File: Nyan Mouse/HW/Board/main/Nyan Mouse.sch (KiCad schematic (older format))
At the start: 11 parts, among them M101 BATTBALANCE-2S, P101 CONN_20X2, P102 CONN_4, P103 CONN_2, P104 CONN_2, U101 DRV8837, U102 DRV8837

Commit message: Finalized connector structure.
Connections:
- net +3.3VA: now also P101.1 (P1), P101.3 (P3), P101.5 (P5); no longer P101.19 (P19), P101.21 (P21), P101.23 (P23)
- net +3.3VD: now also P101.2 (P2), P101.4 (P4), P101.6 (P6); no longer P101.36 (P36), P101.38 (P38), P101.40 (P40)
- net AGND: now also P101.35 (P35), P101.37 (P37); no longer P101.25
- net DGND: now also P101.36 (P36), P101.38 (P38), P101.40 (P40); no longer P101.1 (P1), P101.3 (P3), P101.5 (P5)
- net connectors and lights/RCLK: now also P101.16 (P16); no longer P101.8 (P8)
- net connectors and lights/SCLK: now also P101.14 (P14); no longer P101.6 (P6)
- net connectors and lights/SDI: now also P101.12 (P12); no longer P101.4 (P4)
- net connectors and lights/nOE: now also P101.10 (P10); no longer P101.2 (P2)
- net re1: now also P101.21 (P21); no longer P101.27 (P27)
- net re2: now also P101.23 (P23); no longer P101.29 (P29)
- net re3: now also P101.25; no longer P101.31 (P31)
- net re4: now also P101.27 (P27); no longer P101.33 (P33)
- net re5: now also P101.29 (P29); no longer P101.35 (P35)
- net re6: now also P101.31 (P31); no longer P101.37 (P37)
- net at P101.11 (P11): no longer U102.6 (IN1)
- net at P102.3 (P3): now also P101.18 (P18); no longer P101.12 (P12)
- net at P101.13 (P13): no longer U102.5 (IN2)
- net at P102.4 (P4): now also P101.20 (P20); no longer P101.14 (P14)
- net at P101.28 (P28): now also U101.6 (IN1)
- net at P101.30 (P30): now also U101.5 (IN2)
- net at P101.32 (P32): now also U102.6 (IN1)
- net at P101.34 (P34): now also U102.5 (IN2)
- net at P101.7 (P7): no longer U101.6 (IN1)
- net at P101.9 (P9): no longer U101.5 (IN2)
- new net gyro_a: P101.33 (P33)
- no-connect marks 14 -> 8
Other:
- moved on the sheet: C101, C102, L101, M101, P102, P103, P104, R101, U101, U102

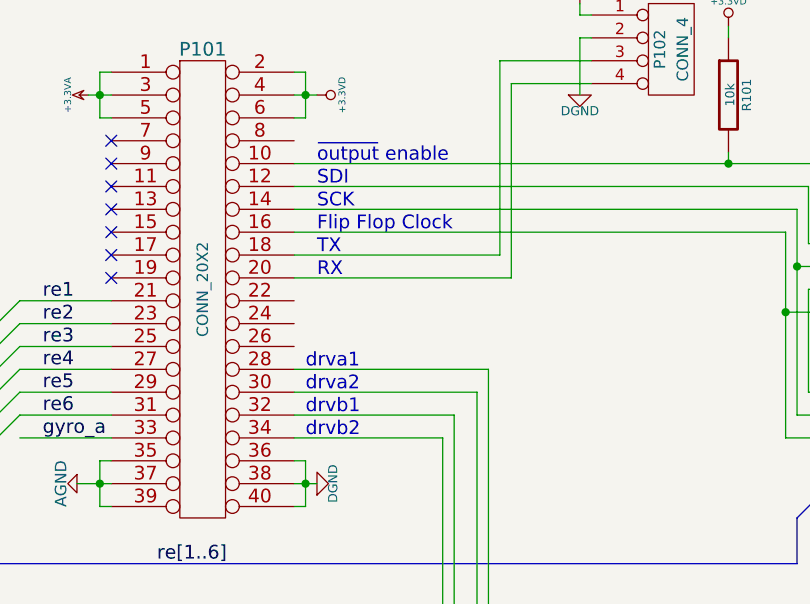
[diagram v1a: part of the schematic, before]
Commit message: Okay, now the connector is finalized.
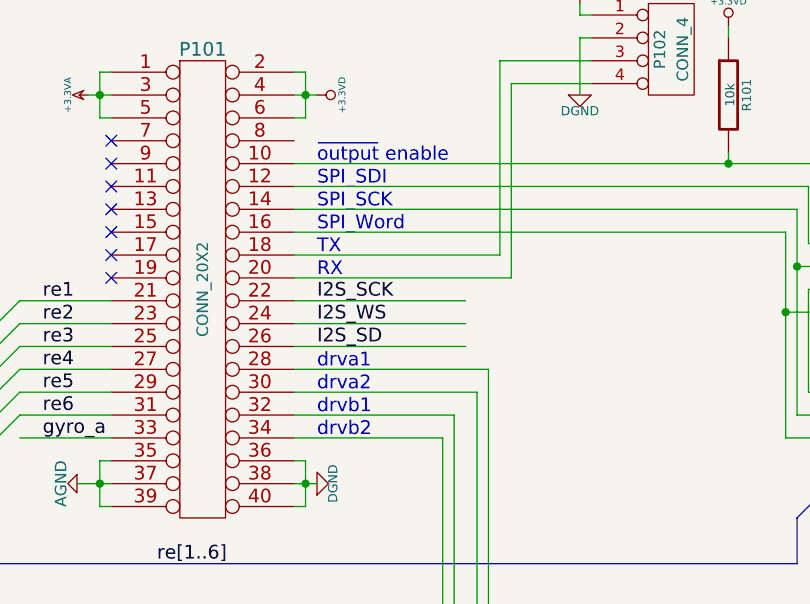
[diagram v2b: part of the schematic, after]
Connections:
- net labels added: I2S_SCK, I2S_SD, I2S_WS
- wire segments 109 -> 112
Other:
- note added: "SPI_SCK"
- note added: "SPI_SDI"
- note added: "SPI_Word"
- note removed: "Flip Flop Clock"
- note removed: "SCK"
- note removed: "SDI"
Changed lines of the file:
@@
 ~output enable
 Text Notes 6500 2100 0    60   ~ 0
-SDI
+SPI_SDI
 Text Notes 6500 2200 0    60   ~ 0
-SCK
+SPI_SCK
 Text Notes 6500 2300 0    60   ~ 0
-Flip Flop Clock
+SPI_Word
 Text Label 5300 2600 0    60   ~ 0
 re1
@@
 Wire Wire Line
 	9250 5950 9250 6000
-Text Notes 6450 3200 0    60   ~ 0
+Text Notes 6500 3200 0    60   ~ 0
 drvb2
-Text Notes 6450 3100 0    60   ~ 0
+Text Notes 6500 3100 0    60   ~ 0
 drvb1
-Text Notes 6450 3000 0    60   ~ 0
+Text Notes 6500 3000 0    60   ~ 0
 drva2
-Text Notes 6450 2900 0    60   ~ 0
+Text Notes 6500 2900 0    60   ~ 0
 drva1
 $Comp
@@
 NoConn ~ 5600 2400
 NoConn ~ 5600 2500
+Wire Wire Line
+	6400 2600 7150 2600
+Wire Wire Line
+	6400 2700 7150 2700
+Wire Wire Line
+	6400 2800 7150 2800
+Text Label 6500 2600 0    60   ~ 0
+I2S_SCK
+Text Label 6500 2700 0    60   ~ 0
+I2S_WS
+Text Label 6500 2800 0    60   ~ 0
+I2S_SD
 $EndSCHEMATC

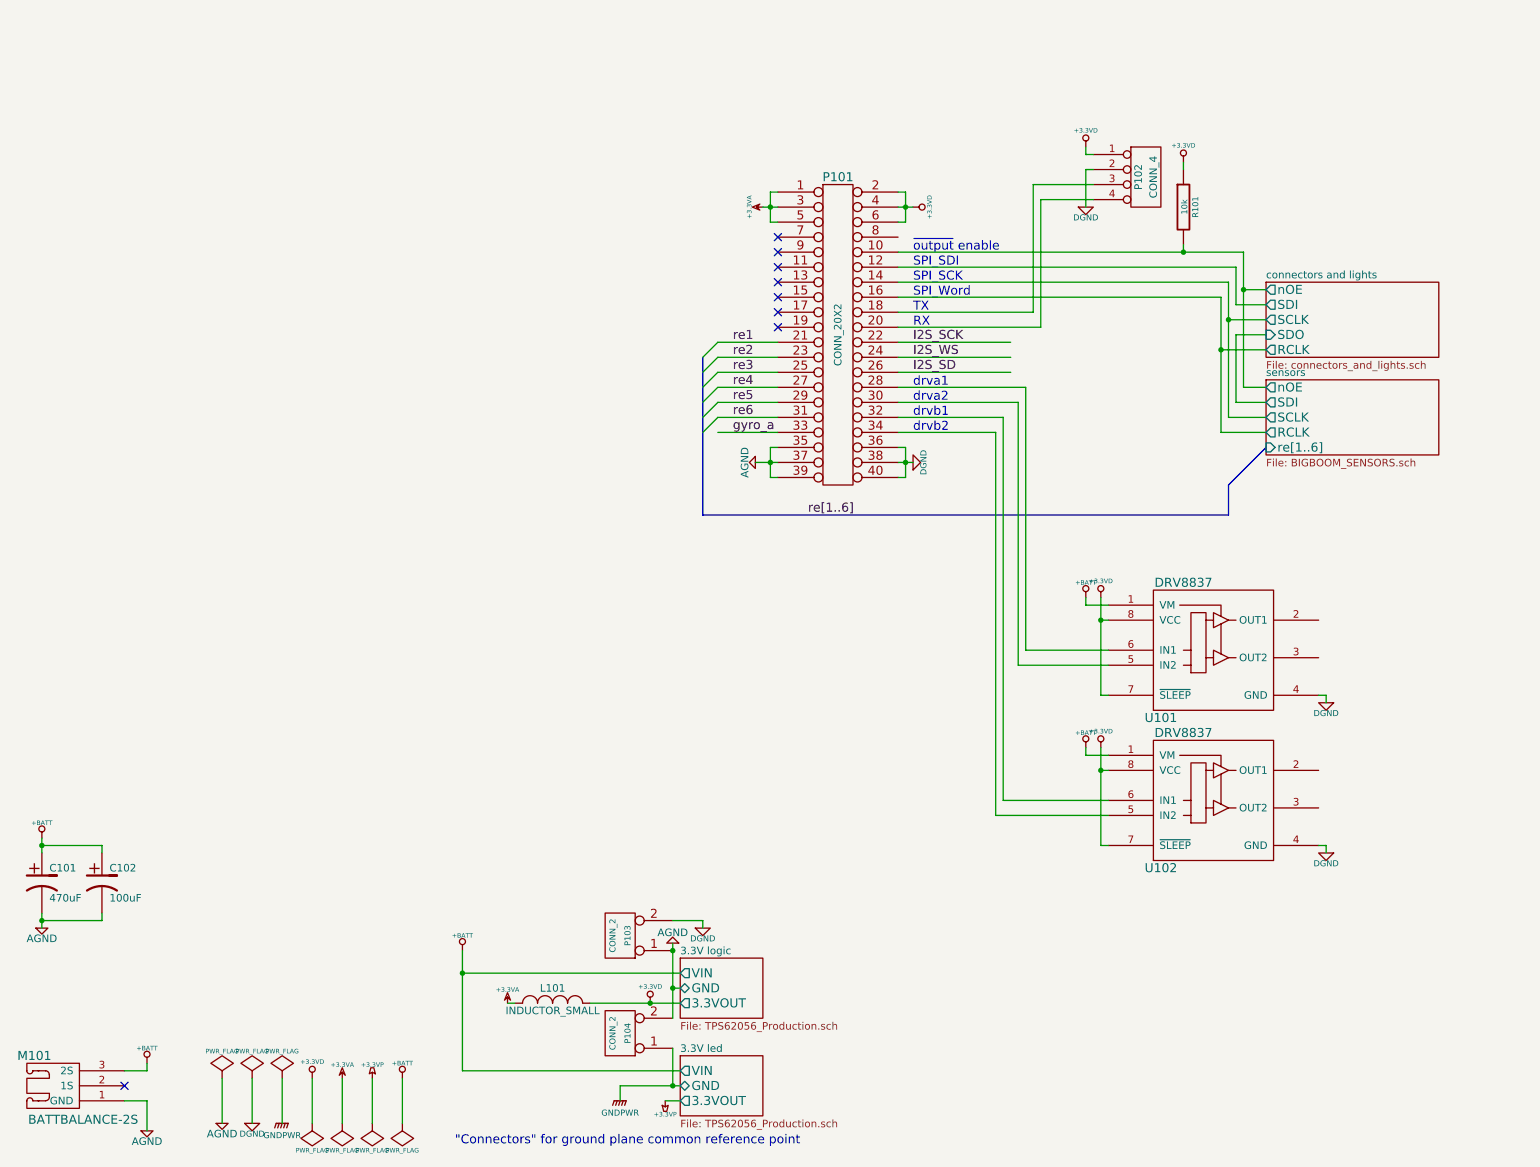
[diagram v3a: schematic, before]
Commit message: Added bank names to FPGA
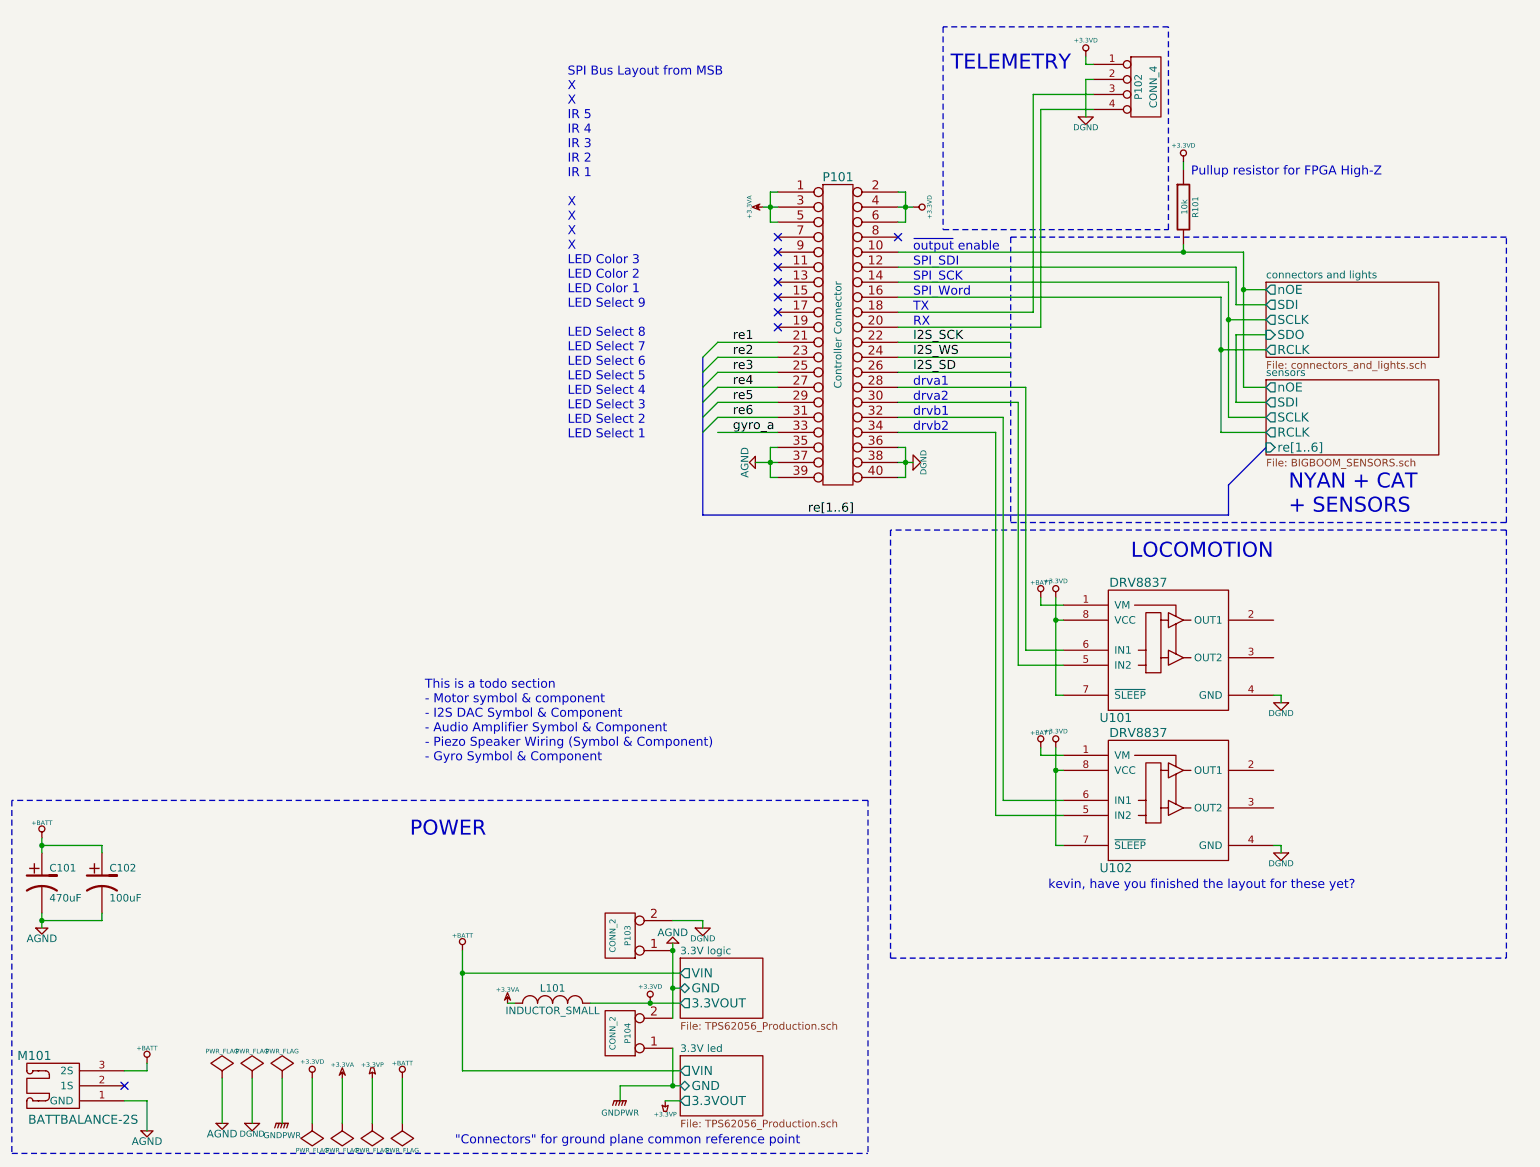
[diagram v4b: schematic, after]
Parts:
- P101: value CONN_20X2 -> Controller Connector
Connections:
- no-connect marks 8 -> 9
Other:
- note added: "LOCOMOTION"
- note added: "NYAN + CAT\n+ SENSORS"
- note added: "POWER"
- note added: "Pullup resistor for FPGA High-Z"
- note added: "SPI Bus Layout from MSB\nX\nX\nIR 5\nIR 4\nIR 3\nIR 2\nIR 1\n\nX\nX\nX\nX\nLED Color 3\nLED Color 2\nLED Color 1\nLED Select 9\n\nLED Select 8\nLED Select 7\nLED Select 6\nLED Select 5\nLED Select 4\nLED Select 3\nLED Select 2\nLED Select 1"
- note added: "TELEMETRY"
- note added: "This is a todo section\n- Motor symbol & component\n- I2S DAC Symbol & Component\n- Audio Amplifier Symbol & Component\n- Piezo Speaker Wiring (Symbol & Component)\n- Gyro Symbol & Component"
- note added: "kevin, have you finished the layout for these yet?"
- moved on the sheet: P102, U101, U102
